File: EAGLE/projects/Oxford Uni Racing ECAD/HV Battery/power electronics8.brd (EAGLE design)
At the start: 165.9 x 104.3 mm, 68 parts, among them IC1 4043D, IC2 SE555D, IC3 4011D, IC6 4011D, K1 T9AS1D12-48=T9A, K2 T9AS5D12-12=T9A, K3 T9AS1D12-48=T9A, K4 T9AS1D12-48=T9A, K5 T9AS1D12-48=T9A, Q1 BSS138, Q2 BSS138, Q3 BSS138, Q4 BSS138, Q5 BSS138

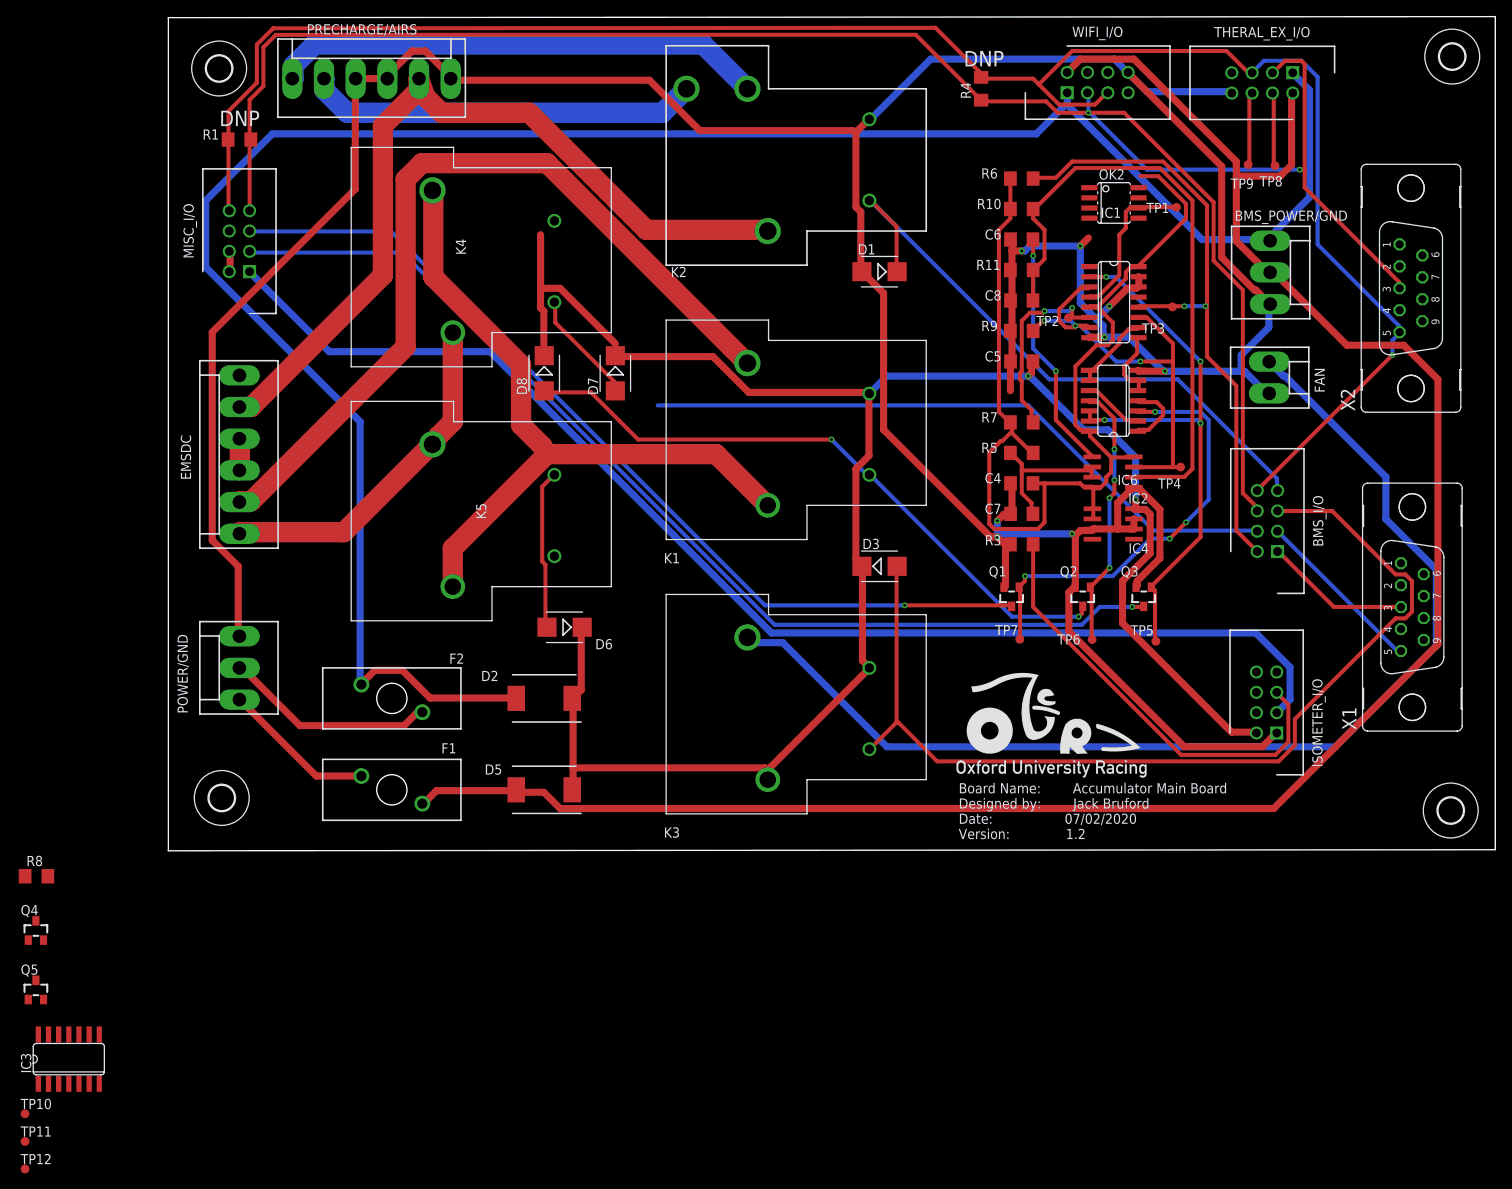
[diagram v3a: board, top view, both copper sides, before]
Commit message: Connected TP11 and 12, mods post DRC and ERC, new board layout and rewired CAN to run in parralel
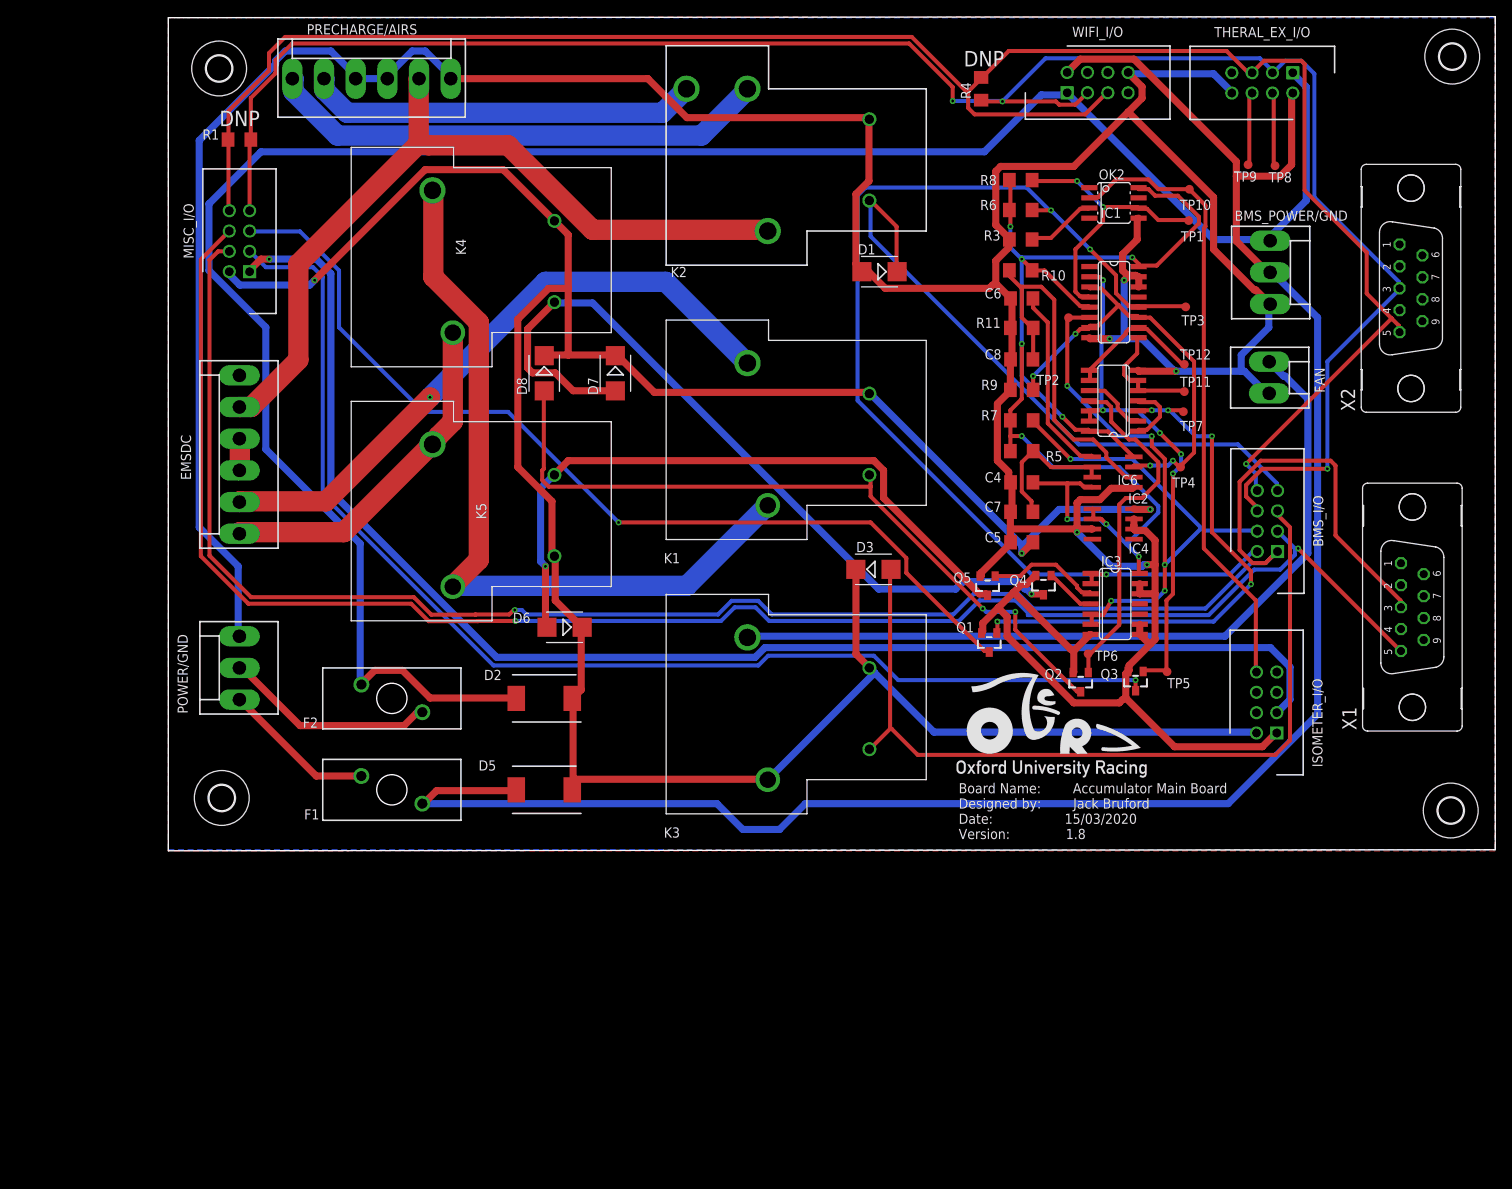
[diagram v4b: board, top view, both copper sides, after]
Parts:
- moved TP10 185.8 mm to (127.6, 82.7)
- moved TP12 176.4 mm to (127.0, 60.8)
- moved TP11 172.6 mm to (127.0, 57.4)
- moved R8 150.7 mm to (106.6, 83.8)
- moved IC3 142.6 mm to (118.4, 30.9), turned to 270 degrees
- moved Q4 133.1 mm to (109.4, 33.2), turned to 180 degrees
- moved Q5 129.2 mm to (102.4, 33.1), turned to 180 degrees
- moved R3 38.1 mm to (106.6, 76.4)
- moved TP7 35.0 mm to (126.9, 54.9)
- moved C5 22.6 mm to (106.7, 38.6)
- moved Q2 10.7 mm to (114.0, 21.1)
- moved Q3 10.6 mm to (120.9, 21.2)
- moved R10 7.66 mm to (106.6, 72.6), turned to 0 degrees
- moved C8 7.37 mm to (106.7, 61.4)
- moved R9 7.37 mm to (106.7, 57.6)
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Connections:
- net GND: now also IC3.12, IC3.13, IC3.8, IC3.9
- net N$10: now also TP11.TP
- net N$13: now also TP12.TP
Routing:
- net CAN1_H: track 18.3 -> 232.1 mm, vias 0 -> 1
- net CAN1_L: track 21.6 -> 211.2 mm, vias 0 -> 2
- net +12V: track 251.1 -> 339.9 mm, vias 2 -> 3
- net N$6: track 14.2 -> 98.9 mm, vias 0 -> 1
- net OK_HS: track 0.00 -> 78.0 mm
- net N$9: track 20.0 -> 84.0 mm, vias 0 -> 1
- net CHARGE_SAFE: track 79.3 -> 140.5 mm, vias 2 -> 3
- net M_HS: track 54.7 -> 0.00 mm
- net FAN+: track 141.3 -> 100.5 mm
- net GND: track 485.1 -> 521.3 mm, vias 8 -> 5
- net N$28: track 77.6 -> 45.7 mm
- net +3V3: track 133.1 -> 160.7 mm, vias 0 -> 9
- net N$15: track 103.7 -> 79.1 mm, vias 0 -> 1
- net FAN_ENABLE: track 124.7 -> 105.1 mm
- net IMD_LED-: track 132.2 -> 151.3 mm
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- added copper zone on layer 1, net GND
- added copper zone on layer 16, net GND
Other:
- board text added: "Board Name: Accumulator Main Board Designed by: Jack Bruford Date: 15/03/2020 Version: 1.8"
- board text removed: "Board Name: Accumulator Main Board Designed by: Jack Bruford Date: 07/02/2020 Version: 1.2"

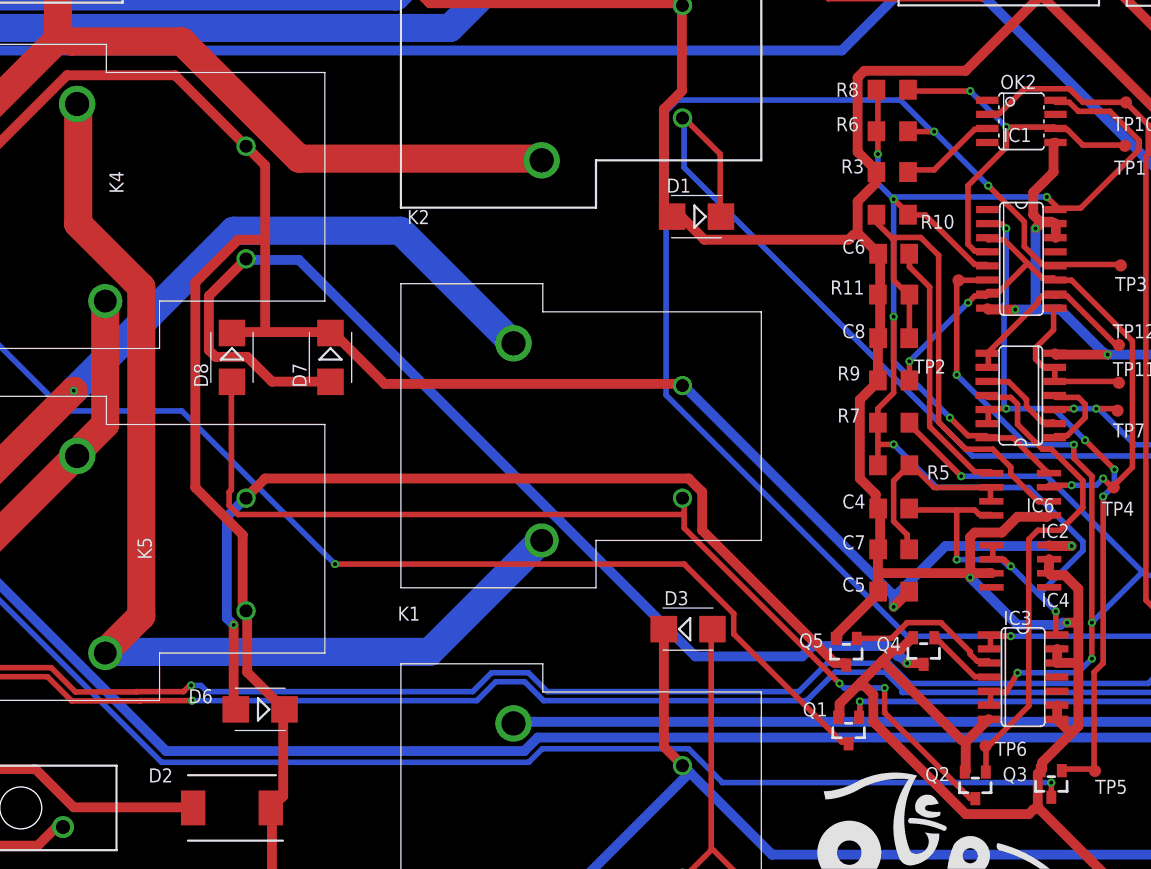
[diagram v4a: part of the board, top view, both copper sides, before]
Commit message: Made edits as suggested by William Matthews and generated Gerber files
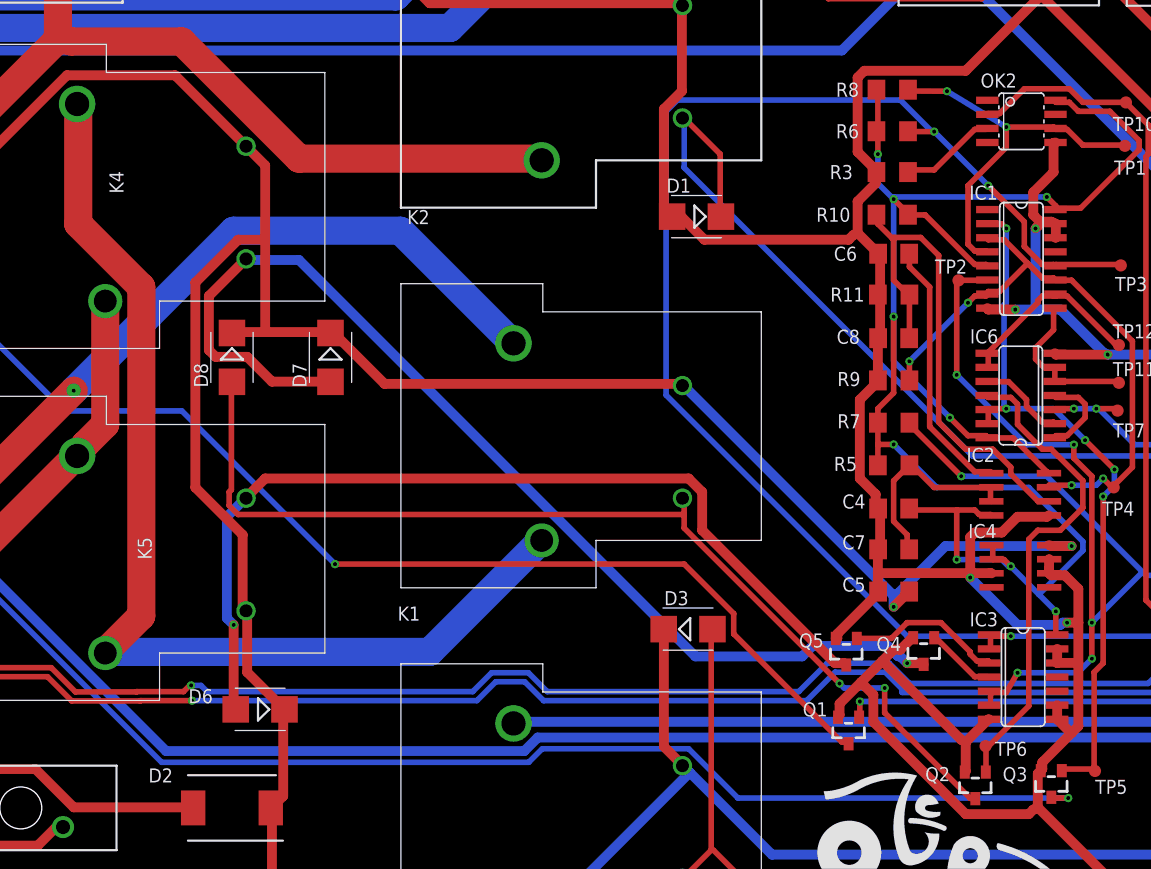
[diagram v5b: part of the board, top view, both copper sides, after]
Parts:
- X1: value (none) -> CAN 1
- X2: value (none) -> CAN 2
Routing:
- net IMD_LED-: track 151.3 -> 153.6 mm
